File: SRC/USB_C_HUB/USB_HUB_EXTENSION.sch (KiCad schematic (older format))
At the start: 7 parts

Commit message: ALL DONE BUT THE HDMI SECTION. NEED FOOTPRINT ASSIGNMENT
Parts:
- IC3: renamed from IC?; footprint QFN50P500X500X100-33N-D -> SamacSys_Parts_2:QFN50P500X500X100-33N-D
- gave numbers to parts that had none: 6
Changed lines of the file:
@@
 $Descr A4 11693 8268
 encoding utf-8
-Sheet 10 11
+Sheet 5 15
 Title ""
 Date ""
@@
 P 5625 1025
 AR Path="/660C6EC5" Ref="C?"  Part="1"
-AR Path="/6609E24E/660C6EC5" Ref="C?"  Part="1"
-F 0 "C?" H 5717 1071 50  0000 L CNN
+AR Path="/6609E24E/660C6EC5" Ref="C63"  Part="1"
+F 0 "C63" H 5717 1071 50  0000 L CNN
 F 1 "4.7" H 5717 980 50  0000 L CNN
 F 2 "" H 5625 1025 50  0001 C CNN
@@
 P 5800 850
 AR Path="/660C6ED5" Ref="#PWR?"  Part="1"
-AR Path="/6609E24E/660C6ED5" Ref="#PWR?"  Part="1"
-F 0 "#PWR?" H 5800 700 50  0001 C CNN
+AR Path="/6609E24E/660C6ED5" Ref="#PWR0153"  Part="1"
+F 0 "#PWR0153" H 5800 700 50  0001 C CNN
 F 1 "+3.3V" H 5650 925 50  0000 C CNN
 F 2 "" H 5800 850 60  0000 C CNN
@@
 P 4425 1050
 AR Path="/660C6EDD" Ref="#PWR?"  Part="1"
-AR Path="/6609E24E/660C6EDD" Ref="#PWR?"  Part="1"
-F 0 "#PWR?" H 4425 900 50  0001 C CNN
+AR Path="/6609E24E/660C6EDD" Ref="#PWR0154"  Part="1"
+F 0 "#PWR0154" H 4425 900 50  0001 C CNN
 F 1 "+3.3V" H 4275 1125 50  0000 C CNN
 F 2 "" H 4425 1050 60  0000 C CNN
@@
 AR Path="/619540C6/660C6EE9" Ref="#PWR?"  Part="1"
 AR Path="/660C6EE9" Ref="#PWR?"  Part="1"
-AR Path="/6609E24E/660C6EE9" Ref="#PWR?"  Part="1"
-F 0 "#PWR?" H 3400 2400 50  0001 C CNN
+AR Path="/6609E24E/660C6EE9" Ref="#PWR0155"  Part="1"
+F 0 "#PWR0155" H 3400 2400 50  0001 C CNN
 F 1 "GND" H 3405 2477 50  0000 C CNN
 F 2 "" H 3400 2650 60  0000 C CNN
@@
 AR Path="/619540C6/660C6EEF" Ref="#PWR?"  Part="1"
 AR Path="/660C6EEF" Ref="#PWR?"  Part="1"
-AR Path="/6609E24E/660C6EEF" Ref="#PWR?"  Part="1"
-F 0 "#PWR?" H 5850 975 50  0001 C CNN
+AR Path="/6609E24E/660C6EEF" Ref="#PWR0156"  Part="1"
+F 0 "#PWR0156" H 5850 975 50  0001 C CNN
 F 1 "GND" H 5855 1052 50  0000 C CNN
 F 2 "" H 5850 1225 60  0000 C CNN
@@
 AR Path="/619540C6/660C6EF5" Ref="#PWR?"  Part="1"
 AR Path="/660C6EF5" Ref="#PWR?"  Part="1"
-AR Path="/6609E24E/660C6EF5" Ref="#PWR?"  Part="1"
-F 0 "#PWR?" H 4500 4450 50  0001 C CNN
+AR Path="/6609E24E/660C6EF5" Ref="#PWR0157"  Part="1"
+F 0 "#PWR0157" H 4500 4450 50  0001 C CNN
 F 1 "GND" H 4505 4527 50  0000 C CNN
 F 2 "" H 4500 4700 60  0000 C CNN
@@
 AR Path="/619540C6/660C6F03" Ref="#PWR?"  Part="1"
 AR Path="/660C6F03" Ref="#PWR?"  Part="1"
-AR Path="/6609E24E/660C6F03" Ref="#PWR?"  Part="1"
-F 0 "#PWR?" H 5650 2875 50  0001 C CNN
+AR Path="/6609E24E/660C6F03" Ref="#PWR0158"  Part="1"
+F 0 "#PWR0158" H 5650 2875 50  0001 C CNN
 F 1 "GND" H 5655 2952 50  0000 C CNN
 F 2 "" H 5650 3125 60  0000 C CNN
@@
 AR Path="/619540C6/660C6F0A" Ref="#PWR?"  Part="1"
 AR Path="/660C6F0A" Ref="#PWR?"  Part="1"
-AR Path="/6609E24E/660C6F0A" Ref="#PWR?"  Part="1"
-F 0 "#PWR?" H 3175 3075 50  0001 C CNN
+AR Path="/6609E24E/660C6F0A" Ref="#PWR0159"  Part="1"
+F 0 "#PWR0159" H 3175 3075 50  0001 C CNN
 F 1 "GND" H 3180 3152 50  0000 C CNN
 F 2 "" H 3175 3325 60  0000 C CNN
@@
 P 3600 2175
 AR Path="/660C6F19" Ref="IC?"  Part="1"
-AR Path="/6609E24E/660C6F19" Ref="IC?"  Part="1"
-F 0 "IC?" H 4600 2625 50  0000 C CNN
+AR Path="/6609E24E/660C6F19" Ref="IC3"  Part="1"
+F 0 "IC3" H 4600 2625 50  0000 C CNN
 F 1 "TUSB2046BIRHBT" H 4550 2525 50  0000 C CNN
-F 2 "QFN50P500X500X100-33N-D" H 5250 3075 50  0001 L CNN
+F 2 "SamacSys_Parts_2:QFN50P500X500X100-33N-D" H 5250 3075 50  0001 L CNN
 F 3 "http://www.ti.com/lit/gpn/TUSB2046B" H 5250 2975 50  0001 L CNN
 F 4 "Texas Instruments TUSB2046BIRHBT, USB Transceiver 5-port at 12Mbit/s, 3.3 V, 32-Pin QFN" H 5250 2875 50  0001 L CNN "Description"
@@
 P 5975 1025
 AR Path="/660D9F3B" Ref="C?"  Part="1"
-AR Path="/6609E24E/660D9F3B" Ref="C?"  Part="1"
-F 0 "C?" H 6067 1071 50  0000 L CNN
+AR Path="/6609E24E/660D9F3B" Ref="C64"  Part="1"
+F 0 "C64" H 6067 1071 50  0000 L CNN
 F 1 "4.7" H 6067 980 50  0000 L CNN
 F 2 "" H 5975 1025 50  0001 C CNN
@@
 	5850 1225 5975 1225
 $Comp
-L Device:Crystal Y?
+L Device:Crystal Y2
 U 1 1 66183BA4
 P 2025 2225
-F 0 "Y?" V 1979 2356 50  0000 L CNN
+F 0 "Y2" V 1979 2356 50  0000 L CNN
 F 1 "6MHz" V 2070 2356 50  0000 L CNN
 F 2 "" H 2025 2225 50  0001 C CNN
@@
 $EndComp
 $Comp
-L Device:C_Small C?
+L Device:C_Small C62
 U 1 1 66184A38
 P 1600 1925
-F 0 "C?" V 1371 1925 50  0000 C CNN
+F 0 "C62" V 1371 1925 50  0000 C CNN
 F 1 "22pF" V 1462 1925 50  0000 C CNN
 F 2 "" H 1600 1925 50  0001 C CNN
@@
 $EndComp
 $Comp
-L Device:C_Small C?
+L Device:C_Small C61
 U 1 1 661850C0
 P 1575 2475
-F 0 "C?" V 1346 2475 50  0000 C CNN
+F 0 "C61" V 1346 2475 50  0000 C CNN
 F 1 "22pF" V 1437 2475 50  0000 C CNN
 F 2 "" H 1575 2475 50  0001 C CNN
@@
 P 3225 1050
 AR Path="/66188D48" Ref="#PWR?"  Part="1"
-AR Path="/6609E24E/66188D48" Ref="#PWR?"  Part="1"
-F 0 "#PWR?" H 3225 900 50  0001 C CNN
+AR Path="/6609E24E/66188D48" Ref="#PWR0160"  Part="1"
+F 0 "#PWR0160" H 3225 900 50  0001 C CNN
 F 1 "+3.3V" H 3075 1125 50  0000 C CNN
 F 2 "" H 3225 1050 60  0000 C CNN
@@
 P 3225 1250
 AR Path="/661895DC" Ref="R?"  Part="1"
-AR Path="/6609E24E/661895DC" Ref="R?"  Part="1"
-F 0 "R?" H 3293 1296 50  0000 L CNN
+AR Path="/6609E24E/661895DC" Ref="R54"  Part="1"
+F 0 "R54" H 3293 1296 50  0000 L CNN
 F 1 "10K" H 3293 1205 50  0000 L CNN
 F 2 "" V 3265 1240 50  0001 C CNN
@@
 P 6050 2550
 AR Path="/6618E091" Ref="#PWR?"  Part="1"
-AR Path="/6609E24E/6618E091" Ref="#PWR?"  Part="1"
-F 0 "#PWR?" H 6050 2400 50  0001 C CNN
+AR Path="/6609E24E/6618E091" Ref="#PWR0161"  Part="1"
+F 0 "#PWR0161" H 6050 2400 50  0001 C CNN
 F 1 "+3.3V" H 5900 2625 50  0000 C CNN
 F 2 "" H 6050 2550 60  0000 C CNN
@@
 AR Path="/619540C6/66191B78" Ref="#PWR?"  Part="1"
 AR Path="/66191B78" Ref="#PWR?"  Part="1"
-AR Path="/6609E24E/66191B78" Ref="#PWR?"  Part="1"
-F 0 "#PWR?" H 5625 2225 50  0001 C CNN
+AR Path="/6609E24E/66191B78" Ref="#PWR0162"  Part="1"
+F 0 "#PWR0162" H 5625 2225 50  0001 C CNN
 F 1 "GND" H 5525 2375 50  0000 C CNN
 F 2 "" H 5625 2475 60  0000 C CNN

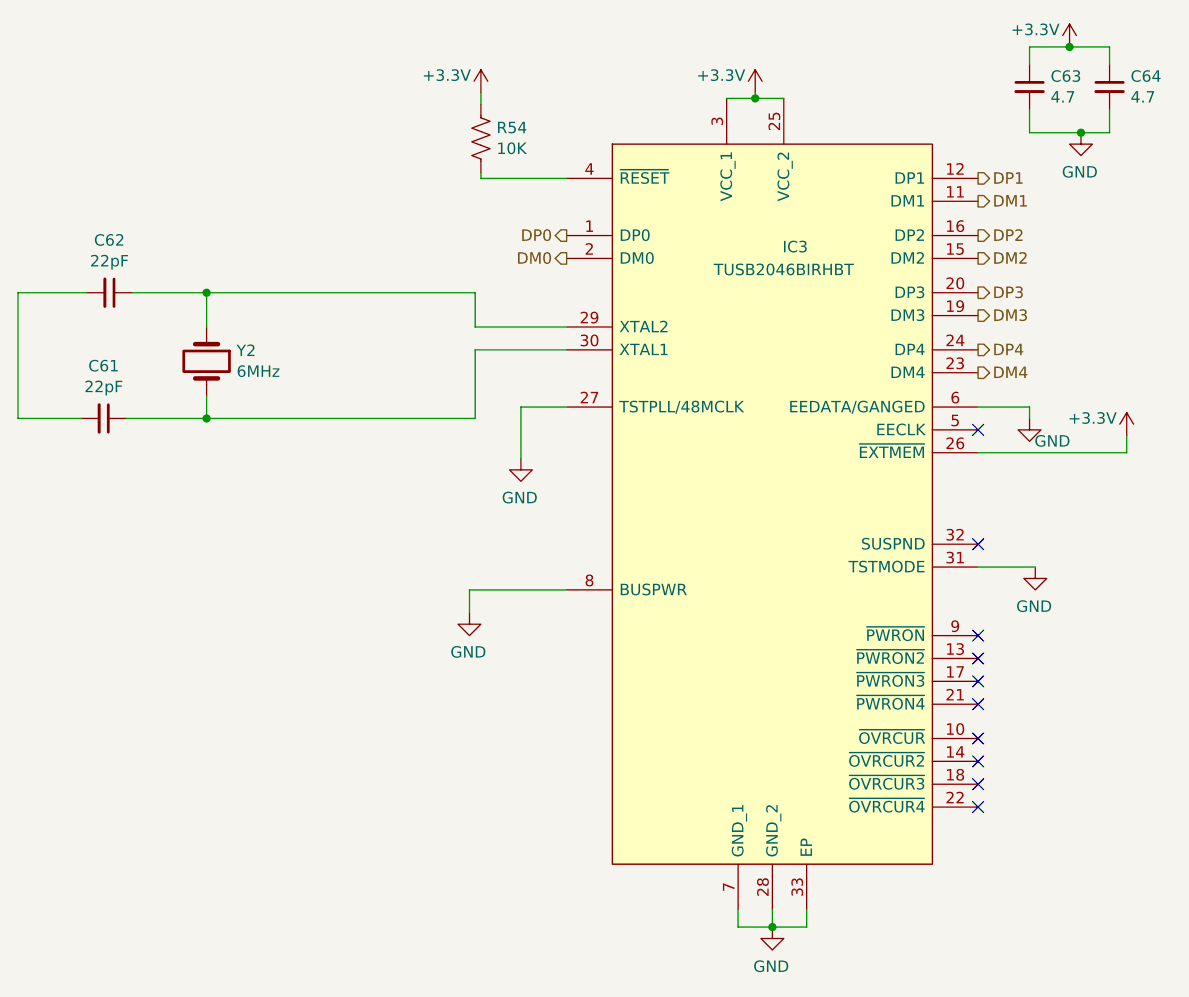
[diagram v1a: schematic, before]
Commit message: schematic capture complete. Pending Footprint assignment. accetable Errors=21
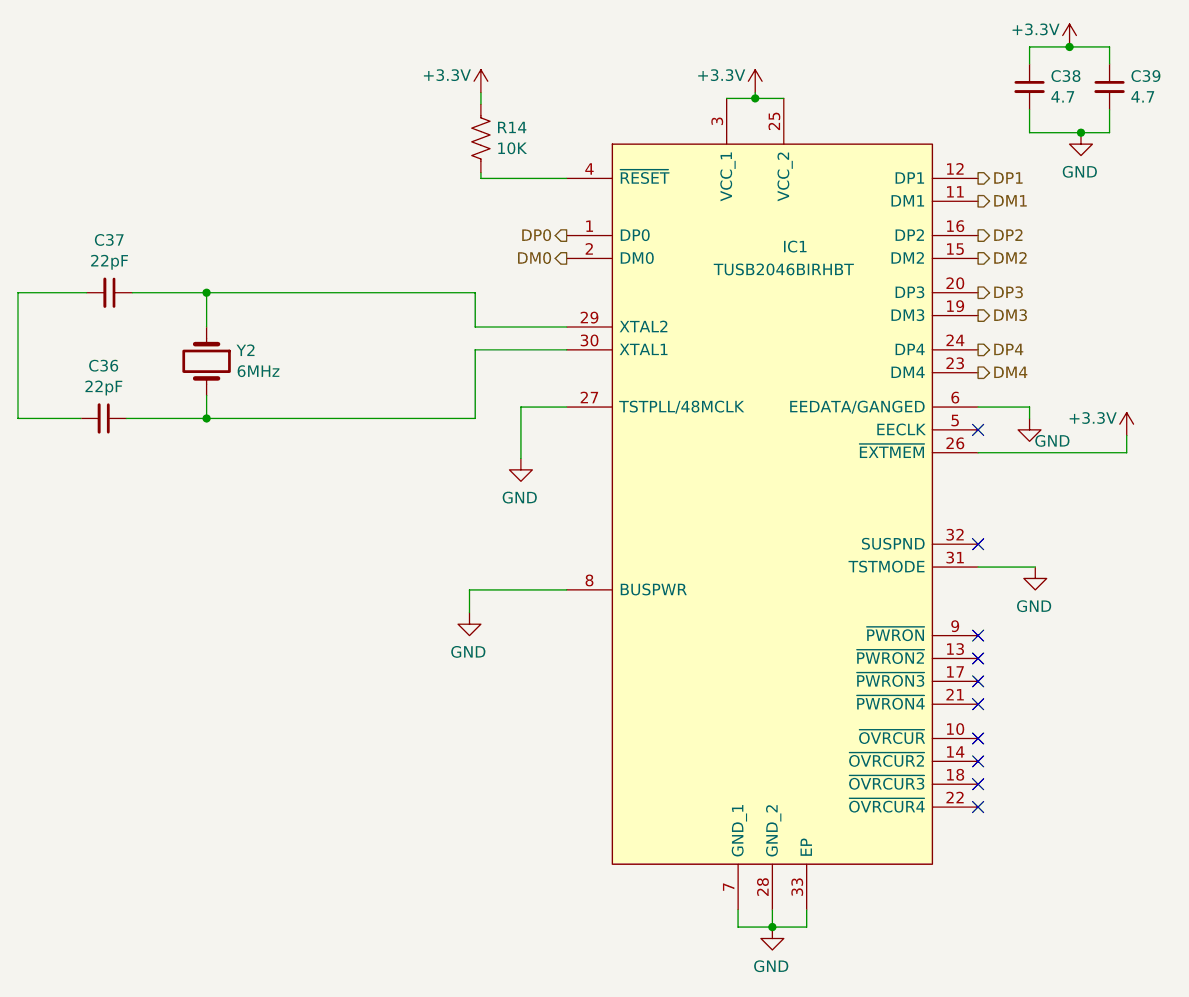
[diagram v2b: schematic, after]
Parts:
- renumbered C61 to C36, C62 to C37, C63 to C38, C64 to C39, IC3 to IC1, R54 to R14
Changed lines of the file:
@@
 P 5625 1025
 AR Path="/660C6EC5" Ref="C?"  Part="1"
-AR Path="/6609E24E/660C6EC5" Ref="C63"  Part="1"
-F 0 "C63" H 5717 1071 50  0000 L CNN
+AR Path="/6609E24E/660C6EC5" Ref="C38"  Part="1"
+F 0 "C38" H 5717 1071 50  0000 L CNN
 F 1 "4.7" H 5717 980 50  0000 L CNN
 F 2 "" H 5625 1025 50  0001 C CNN
@@
 P 5800 850
 AR Path="/660C6ED5" Ref="#PWR?"  Part="1"
-AR Path="/6609E24E/660C6ED5" Ref="#PWR0153"  Part="1"
-F 0 "#PWR0153" H 5800 700 50  0001 C CNN
+AR Path="/6609E24E/660C6ED5" Ref="#PWR054"  Part="1"
+F 0 "#PWR054" H 5800 700 50  0001 C CNN
 F 1 "+3.3V" H 5650 925 50  0000 C CNN
 F 2 "" H 5800 850 60  0000 C CNN
@@
 P 4425 1050
 AR Path="/660C6EDD" Ref="#PWR?"  Part="1"
-AR Path="/6609E24E/660C6EDD" Ref="#PWR0154"  Part="1"
-F 0 "#PWR0154" H 4425 900 50  0001 C CNN
+AR Path="/6609E24E/660C6EDD" Ref="#PWR050"  Part="1"
+F 0 "#PWR050" H 4425 900 50  0001 C CNN
 F 1 "+3.3V" H 4275 1125 50  0000 C CNN
 F 2 "" H 4425 1050 60  0000 C CNN
@@
 AR Path="/619540C6/660C6EE9" Ref="#PWR?"  Part="1"
 AR Path="/660C6EE9" Ref="#PWR?"  Part="1"
-AR Path="/6609E24E/660C6EE9" Ref="#PWR0155"  Part="1"
-F 0 "#PWR0155" H 3400 2400 50  0001 C CNN
+AR Path="/6609E24E/660C6EE9" Ref="#PWR049"  Part="1"
+F 0 "#PWR049" H 3400 2400 50  0001 C CNN
 F 1 "GND" H 3405 2477 50  0000 C CNN
 F 2 "" H 3400 2650 60  0000 C CNN
@@
 AR Path="/619540C6/660C6EEF" Ref="#PWR?"  Part="1"
 AR Path="/660C6EEF" Ref="#PWR?"  Part="1"
-AR Path="/6609E24E/660C6EEF" Ref="#PWR0156"  Part="1"
-F 0 "#PWR0156" H 5850 975 50  0001 C CNN
+AR Path="/6609E24E/660C6EEF" Ref="#PWR055"  Part="1"
+F 0 "#PWR055" H 5850 975 50  0001 C CNN
 F 1 "GND" H 5855 1052 50  0000 C CNN
 F 2 "" H 5850 1225 60  0000 C CNN
@@
 AR Path="/619540C6/660C6EF5" Ref="#PWR?"  Part="1"
 AR Path="/660C6EF5" Ref="#PWR?"  Part="1"
-AR Path="/6609E24E/660C6EF5" Ref="#PWR0157"  Part="1"
-F 0 "#PWR0157" H 4500 4450 50  0001 C CNN
+AR Path="/6609E24E/660C6EF5" Ref="#PWR051"  Part="1"
+F 0 "#PWR051" H 4500 4450 50  0001 C CNN
 F 1 "GND" H 4505 4527 50  0000 C CNN
 F 2 "" H 4500 4700 60  0000 C CNN
@@
 AR Path="/619540C6/660C6F03" Ref="#PWR?"  Part="1"
 AR Path="/660C6F03" Ref="#PWR?"  Part="1"
-AR Path="/6609E24E/660C6F03" Ref="#PWR0158"  Part="1"
-F 0 "#PWR0158" H 5650 2875 50  0001 C CNN
+AR Path="/6609E24E/660C6F03" Ref="#PWR053"  Part="1"
+F 0 "#PWR053" H 5650 2875 50  0001 C CNN
 F 1 "GND" H 5655 2952 50  0000 C CNN
 F 2 "" H 5650 3125 60  0000 C CNN
@@
 AR Path="/619540C6/660C6F0A" Ref="#PWR?"  Part="1"
 AR Path="/660C6F0A" Ref="#PWR?"  Part="1"
-AR Path="/6609E24E/660C6F0A" Ref="#PWR0159"  Part="1"
-F 0 "#PWR0159" H 3175 3075 50  0001 C CNN
+AR Path="/6609E24E/660C6F0A" Ref="#PWR047"  Part="1"
+F 0 "#PWR047" H 3175 3075 50  0001 C CNN
 F 1 "GND" H 3180 3152 50  0000 C CNN
 F 2 "" H 3175 3325 60  0000 C CNN
@@
 P 3600 2175
 AR Path="/660C6F19" Ref="IC?"  Part="1"
-AR Path="/6609E24E/660C6F19" Ref="IC3"  Part="1"
-F 0 "IC3" H 4600 2625 50  0000 C CNN
+AR Path="/6609E24E/660C6F19" Ref="IC1"  Part="1"
+F 0 "IC1" H 4600 2625 50  0000 C CNN
 F 1 "TUSB2046BIRHBT" H 4550 2525 50  0000 C CNN
 F 2 "SamacSys_Parts_2:QFN50P500X500X100-33N-D" H 5250 3075 50  0001 L CNN
@@
 P 5975 1025
 AR Path="/660D9F3B" Ref="C?"  Part="1"
-AR Path="/6609E24E/660D9F3B" Ref="C64"  Part="1"
-F 0 "C64" H 6067 1071 50  0000 L CNN
+AR Path="/6609E24E/660D9F3B" Ref="C39"  Part="1"
+F 0 "C39" H 6067 1071 50  0000 L CNN
 F 1 "4.7" H 6067 980 50  0000 L CNN
 F 2 "" H 5975 1025 50  0001 C CNN
@@
 $EndComp
 $Comp
-L Device:C_Small C62
+L Device:C_Small C37
 U 1 1 66184A38
 P 1600 1925
-F 0 "C62" V 1371 1925 50  0000 C CNN
+F 0 "C37" V 1371 1925 50  0000 C CNN
 F 1 "22pF" V 1462 1925 50  0000 C CNN
 F 2 "" H 1600 1925 50  0001 C CNN
@@
 $EndComp
 $Comp
-L Device:C_Small C61
+L Device:C_Small C36
 U 1 1 661850C0
 P 1575 2475
-F 0 "C61" V 1346 2475 50  0000 C CNN
+F 0 "C36" V 1346 2475 50  0000 C CNN
 F 1 "22pF" V 1437 2475 50  0000 C CNN
 F 2 "" H 1575 2475 50  0001 C CNN
@@
 P 3225 1050
 AR Path="/66188D48" Ref="#PWR?"  Part="1"
-AR Path="/6609E24E/66188D48" Ref="#PWR0160"  Part="1"
-F 0 "#PWR0160" H 3225 900 50  0001 C CNN
+AR Path="/6609E24E/66188D48" Ref="#PWR048"  Part="1"
+F 0 "#PWR048" H 3225 900 50  0001 C CNN
 F 1 "+3.3V" H 3075 1125 50  0000 C CNN
 F 2 "" H 3225 1050 60  0000 C CNN
@@
 P 3225 1250
 AR Path="/661895DC" Ref="R?"  Part="1"
-AR Path="/6609E24E/661895DC" Ref="R54"  Part="1"
-F 0 "R54" H 3293 1296 50  0000 L CNN
+AR Path="/6609E24E/661895DC" Ref="R14"  Part="1"
+F 0 "R14" H 3293 1296 50  0000 L CNN
 F 1 "10K" H 3293 1205 50  0000 L CNN
 F 2 "" V 3265 1240 50  0001 C CNN
@@
 P 6050 2550
 AR Path="/6618E091" Ref="#PWR?"  Part="1"
-AR Path="/6609E24E/6618E091" Ref="#PWR0161"  Part="1"
-F 0 "#PWR0161" H 6050 2400 50  0001 C CNN
+AR Path="/6609E24E/6618E091" Ref="#PWR056"  Part="1"
+F 0 "#PWR056" H 6050 2400 50  0001 C CNN
 F 1 "+3.3V" H 5900 2625 50  0000 C CNN
 F 2 "" H 6050 2550 60  0000 C CNN
@@
 AR Path="/619540C6/66191B78" Ref="#PWR?"  Part="1"
 AR Path="/66191B78" Ref="#PWR?"  Part="1"
-AR Path="/6609E24E/66191B78" Ref="#PWR0162"  Part="1"
-F 0 "#PWR0162" H 5625 2225 50  0001 C CNN
+AR Path="/6609E24E/66191B78" Ref="#PWR052"  Part="1"
+F 0 "#PWR052" H 5625 2225 50  0001 C CNN
 F 1 "GND" H 5525 2375 50  0000 C CNN
 F 2 "" H 5625 2475 60  0000 C CNN
